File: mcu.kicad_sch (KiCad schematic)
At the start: 20 parts

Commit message: Split PC_DETECT and POWER_OFF lines
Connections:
- net POWER_OFF: now reaches U?.12 (PA07)
- net PC_DET/POWER_OFF renamed PC_DETECT
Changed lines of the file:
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@@
+    (stroke (width 0) (type default) (color 0 0 0 0))
+  )
+  (wire (pts (xy 117.475 87.63) (xy 138.43 87.63))
     (stroke (width 0) (type default) (color 0 0 0 0))
   )
@@
     (effects (font (size 1.27 1.27)) (justify right))
   )
-  (hierarchical_label "PC_DET{slash}POWER_OFF" (shape output) (at 117.475 140.335 180)
+  (hierarchical_label "PC_DETECT" (shape output) (at 117.475 140.335 180)
     (effects (font (size 1.27 1.27)) (justify right))
   )
@@
     (effects (font (size 1.27 1.27)) (justify right))
   )
+  (hierarchical_label "POWER_OFF" (shape output) (at 117.475 87.63 180)
+    (effects (font (size 1.27 1.27)) (justify right))
+  )

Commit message: Connected ADF7021 chip enable to MCU, grouped PTT/W_DISABLE signal with SWDIO
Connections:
- net PTT/W_DISABLE renamed ADF_CE
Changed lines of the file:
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@@
-    (effects (font (size 1.27 1.27)) (justify right))
-  )
-  (hierarchical_label "PTT{slash}W_DISABLE" (shape input) (at 117.475 99.06 180)
     (effects (font (size 1.27 1.27)) (justify right))
   )
@@
     (effects (font (size 1.27 1.27)) (justify right))
   )
+  (hierarchical_label "ADF_CE" (shape output) (at 117.475 99.06 180)
+    (effects (font (size 1.27 1.27)) (justify right))
+  )

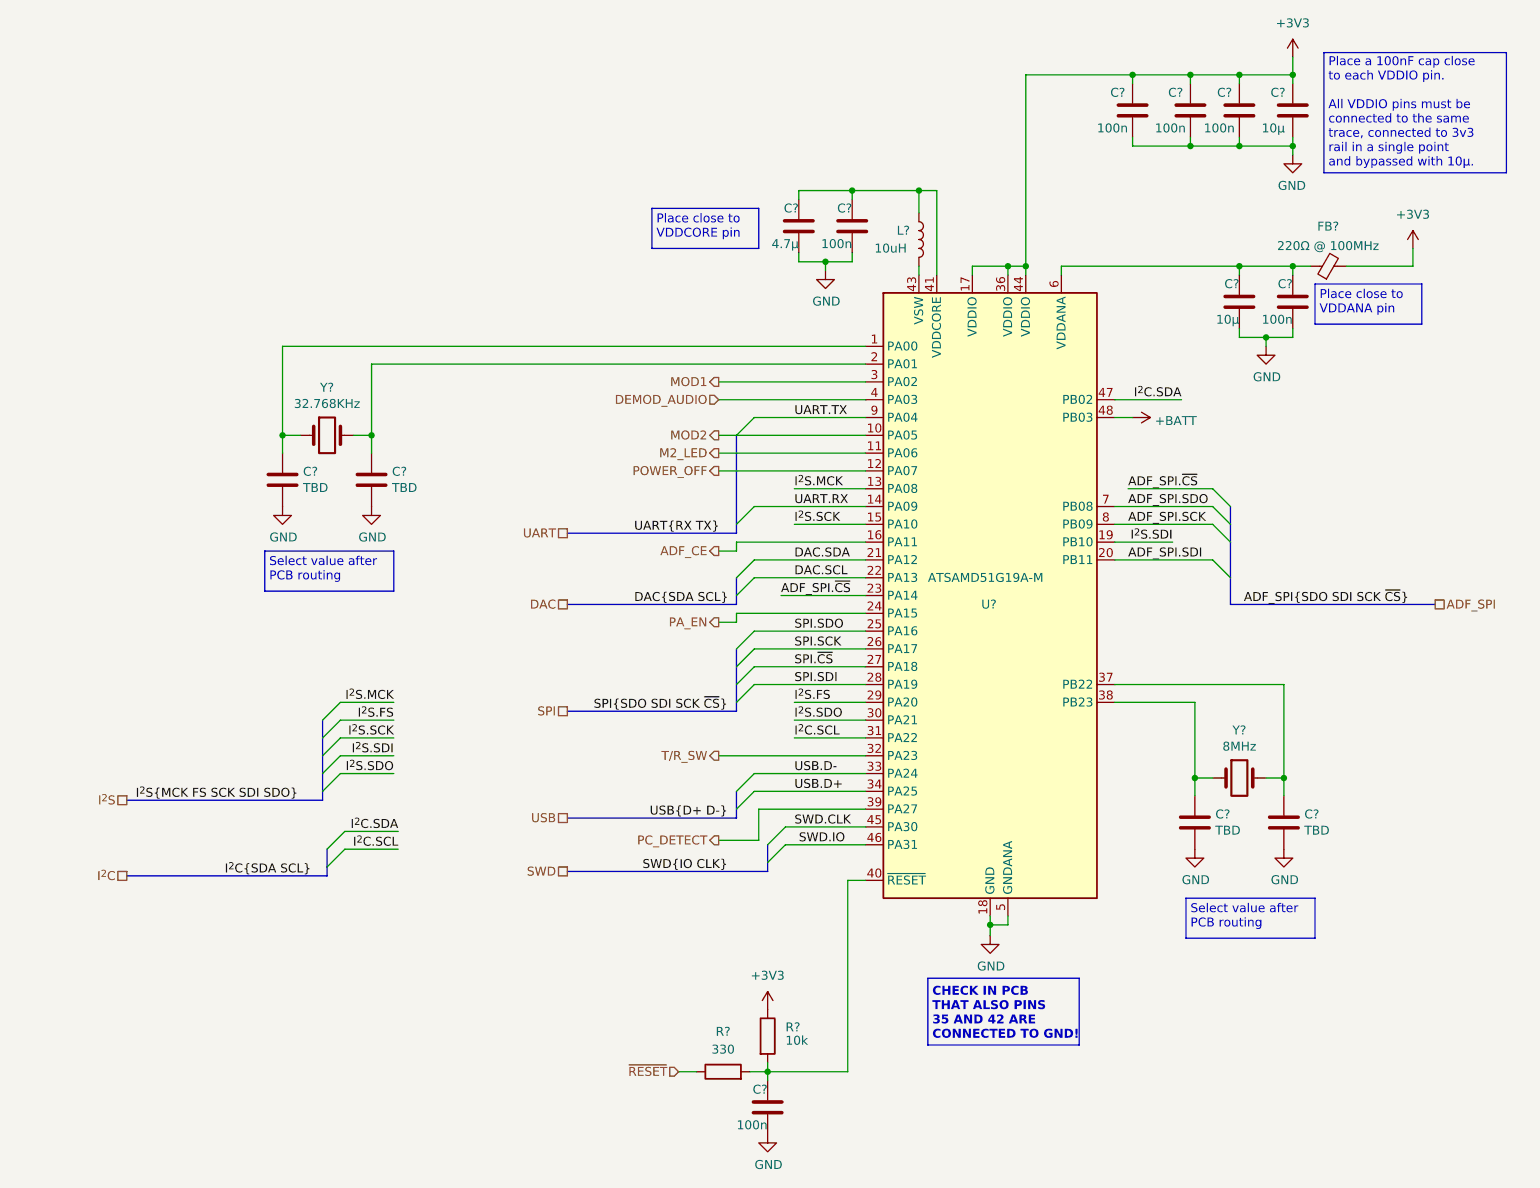
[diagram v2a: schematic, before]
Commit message: Added I2C for external EEPROM on the M.2 connector, added pull-up resistors on the I2C lines
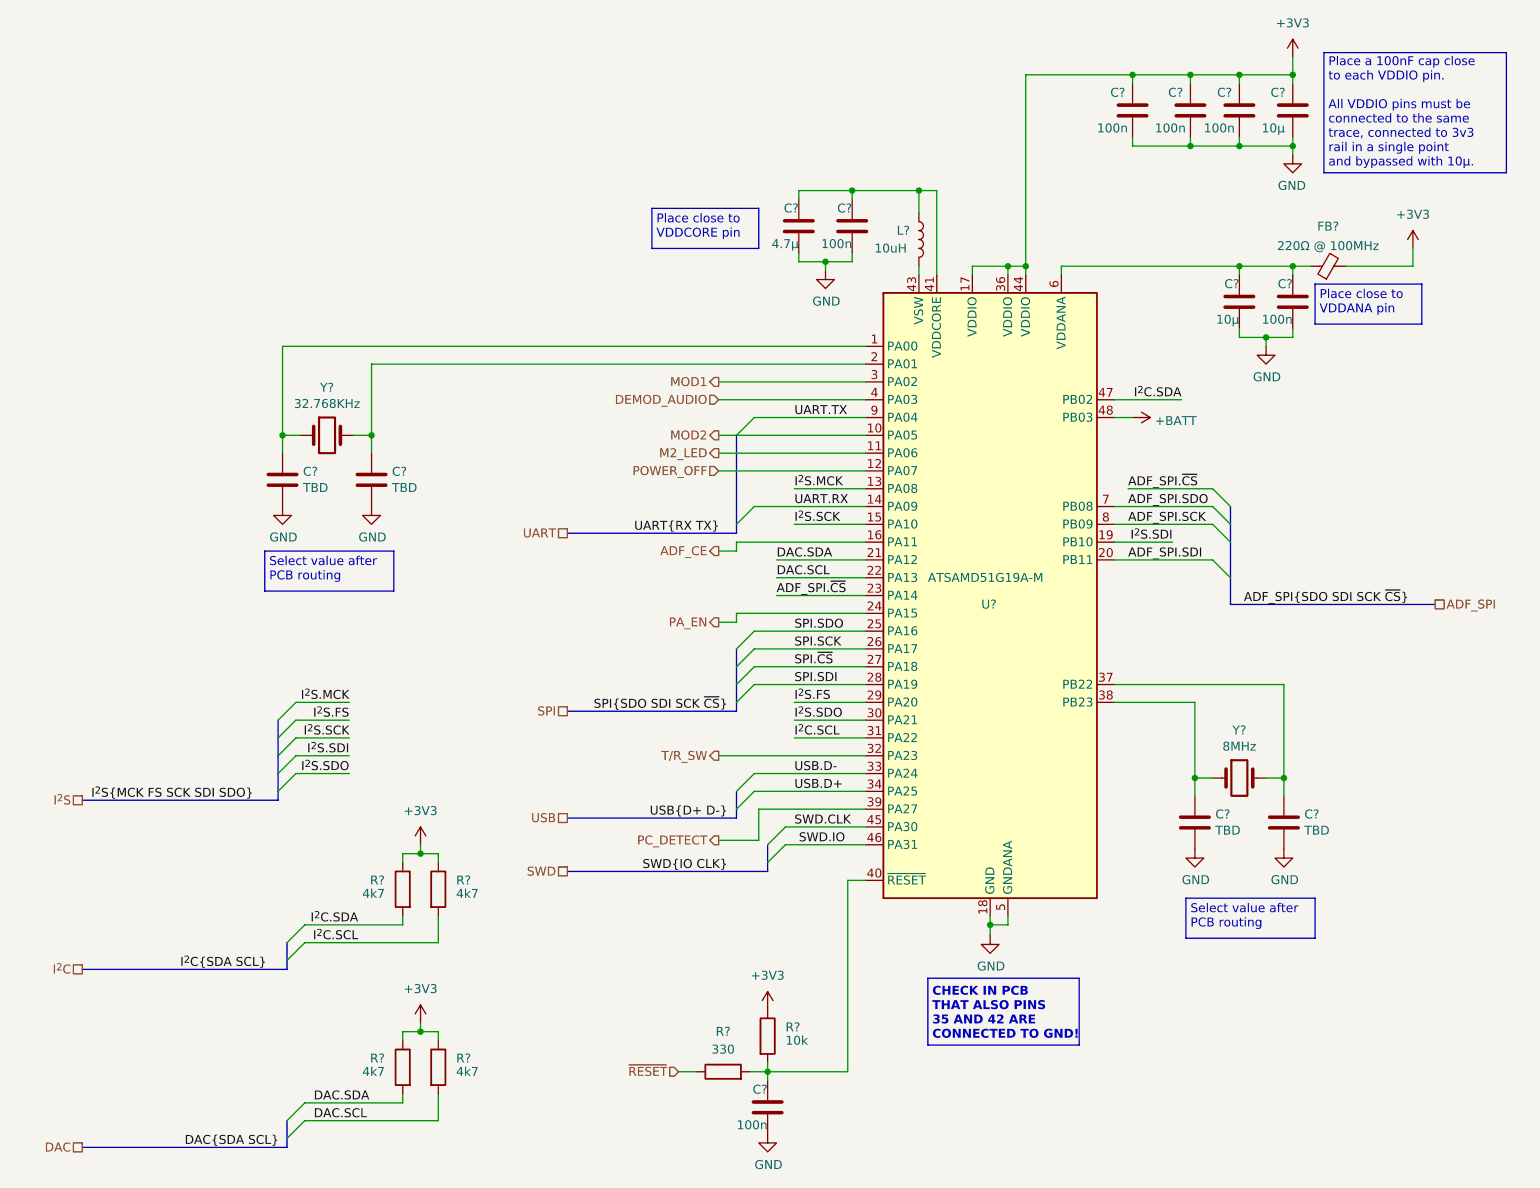
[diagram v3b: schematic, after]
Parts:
- added R? (x4): 4k7, symbol Device:R
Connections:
- net +3V3: now also R?.1, R?.1, R?.1, R?.1
- net DAC.SCL: now also R?.2
- net DAC.SDA: now also R?.2
- net I^{2}C.SCL: now also R?.2
- net I^{2}C.SDA: now also R?.2

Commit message: Set all SMD passive size to 0402
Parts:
- L?: footprint (none) -> Inductor_SMD:L_0402_1005Metric
- R? (x6): footprint (none) -> Resistor_SMD:R_0402_1005Metric
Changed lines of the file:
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@@
       (effects (font (size 1.27 1.27)) (justify left))
     )
-    (property "Footprint" "" (id 2) (at 75.692 147.32 90)
+    (property "Footprint" "Resistor_SMD:R_0402_1005Metric" (id 2) (at 75.692 147.32 90)
       (effects (font (size 1.27 1.27)) hide)
     )
@@
       (effects (font (size 1.27 1.27)) (justify left))
     )
-    (property "Footprint" "" (id 2) (at 122.682 168.275 90)
+    (property "Footprint" "Resistor_SMD:R_0402_1005Metric" (id 2) (at 122.682 168.275 90)
       (effects (font (size 1.27 1.27)) hide)
     )
@@
       (effects (font (size 1.27 1.27)) (justify left))
     )
-    (property "Footprint" "" (id 2) (at 74.168 147.32 90)
+    (property "Footprint" "Resistor_SMD:R_0402_1005Metric" (id 2) (at 74.168 147.32 90)
       (effects (font (size 1.27 1.27)) hide)
     )
@@
     (property "Reference" "R?" (id 0) (at 118.11 167.64 90))
     (property "Value" "330" (id 1) (at 118.11 170.18 90))
-    (property "Footprint" "" (id 2) (at 118.11 175.133 90)
+    (property "Footprint" "Resistor_SMD:R_0402_1005Metric" (id 2) (at 118.11 175.133 90)
       (effects (font (size 1.27 1.27)) hide)
     )
@@
       (effects (font (size 1.27 1.27)) (justify left))
     )
-    (property "Footprint" "" (id 2) (at 74.168 172.72 90)
+    (property "Footprint" "Resistor_SMD:R_0402_1005Metric" (id 2) (at 74.168 172.72 90)
       (effects (font (size 1.27 1.27)) hide)
     )
@@
       (effects (font (size 1.27 1.27)) (justify left))
     )
-    (property "Footprint" "" (id 2) (at 146.05 54.61 0)
+    (property "Footprint" "Inductor_SMD:L_0402_1005Metric" (id 2) (at 146.05 54.61 0)
       (effects (font (size 1.27 1.27)) hide)
     )
@@
       (effects (font (size 1.27 1.27)) (justify left))
     )
-    (property "Footprint" "" (id 2) (at 75.692 172.72 90)
-      (effects (font (size 1.27 1.27)) hide)
-    )
+    (property "Footprint" "Resistor_SMD:R_0402_1005Metric" (id 2) (at 75.692 172.72 90)
+      (effects (font (size 1.27 1.27)) hide)
+    )
